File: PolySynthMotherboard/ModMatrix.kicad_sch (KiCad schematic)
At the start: 160 parts, among them SW501 MM, SW502 MM, SW503 MM, SW504 MM, SW505 MM, SW506 MM, SW507 MM, SW508 MM, SW509 MM, SW510 MM, SW511 MM, SW512 MM, SW513 MM, SW514 MM, SW515 MM, SW516 MM, SW517 MM, SW518 MM, SW519 MM, SW520 MM, SW521 MM, SW522 MM, SW523 MM, SW524 MM, SW525 MM, SW526 MM, SW527 MM, SW528 MM, SW529 MM, SW530 MM, SW531 MM, SW532 MM, SW533 MM, SW534 MM, SW535 MM, SW536 MM, SW537 MM, SW538 MM, SW539 MM, SW540 MM, SW541 MM, SW542 MM, SW543 MM, SW544 MM, SW545 MM, SW546 MM, SW547 MM, SW548 MM, U501 MCP23S17_SS

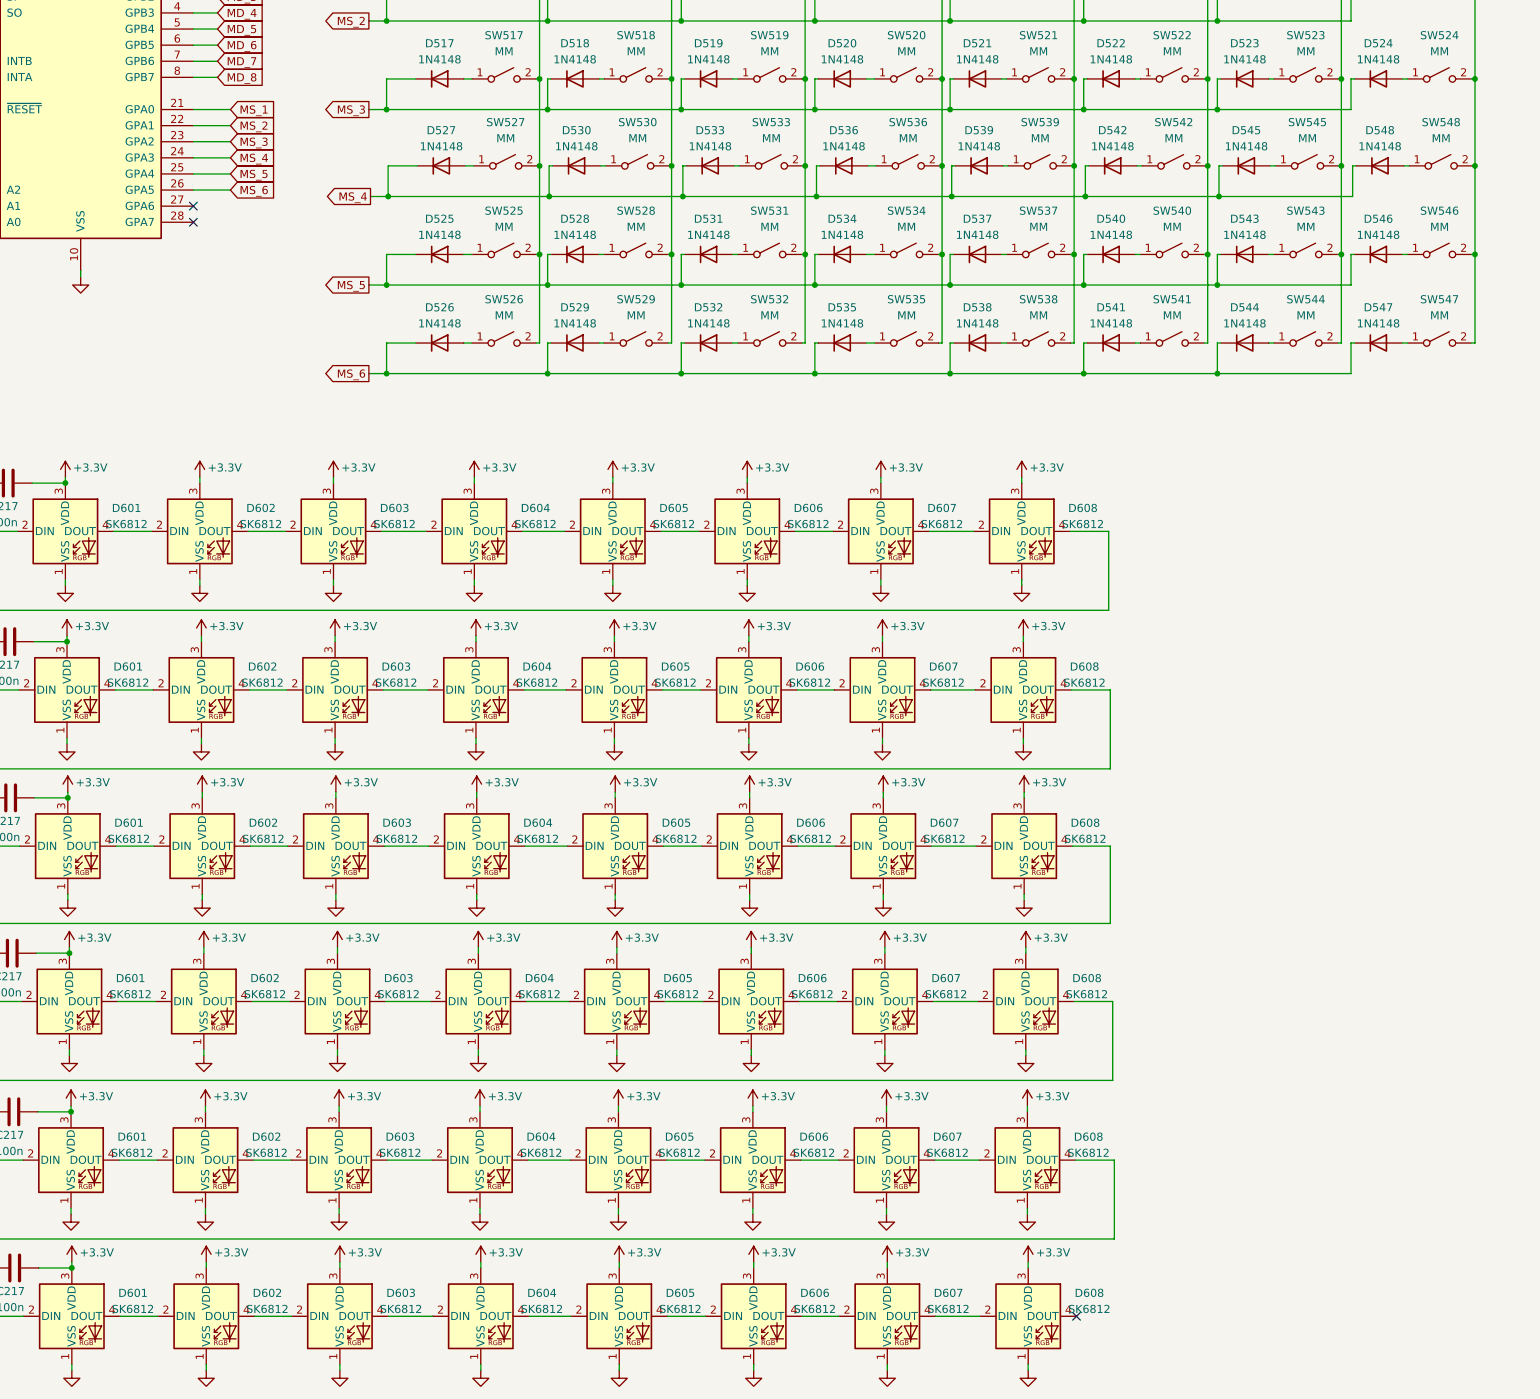
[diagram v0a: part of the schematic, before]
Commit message: net class assignment
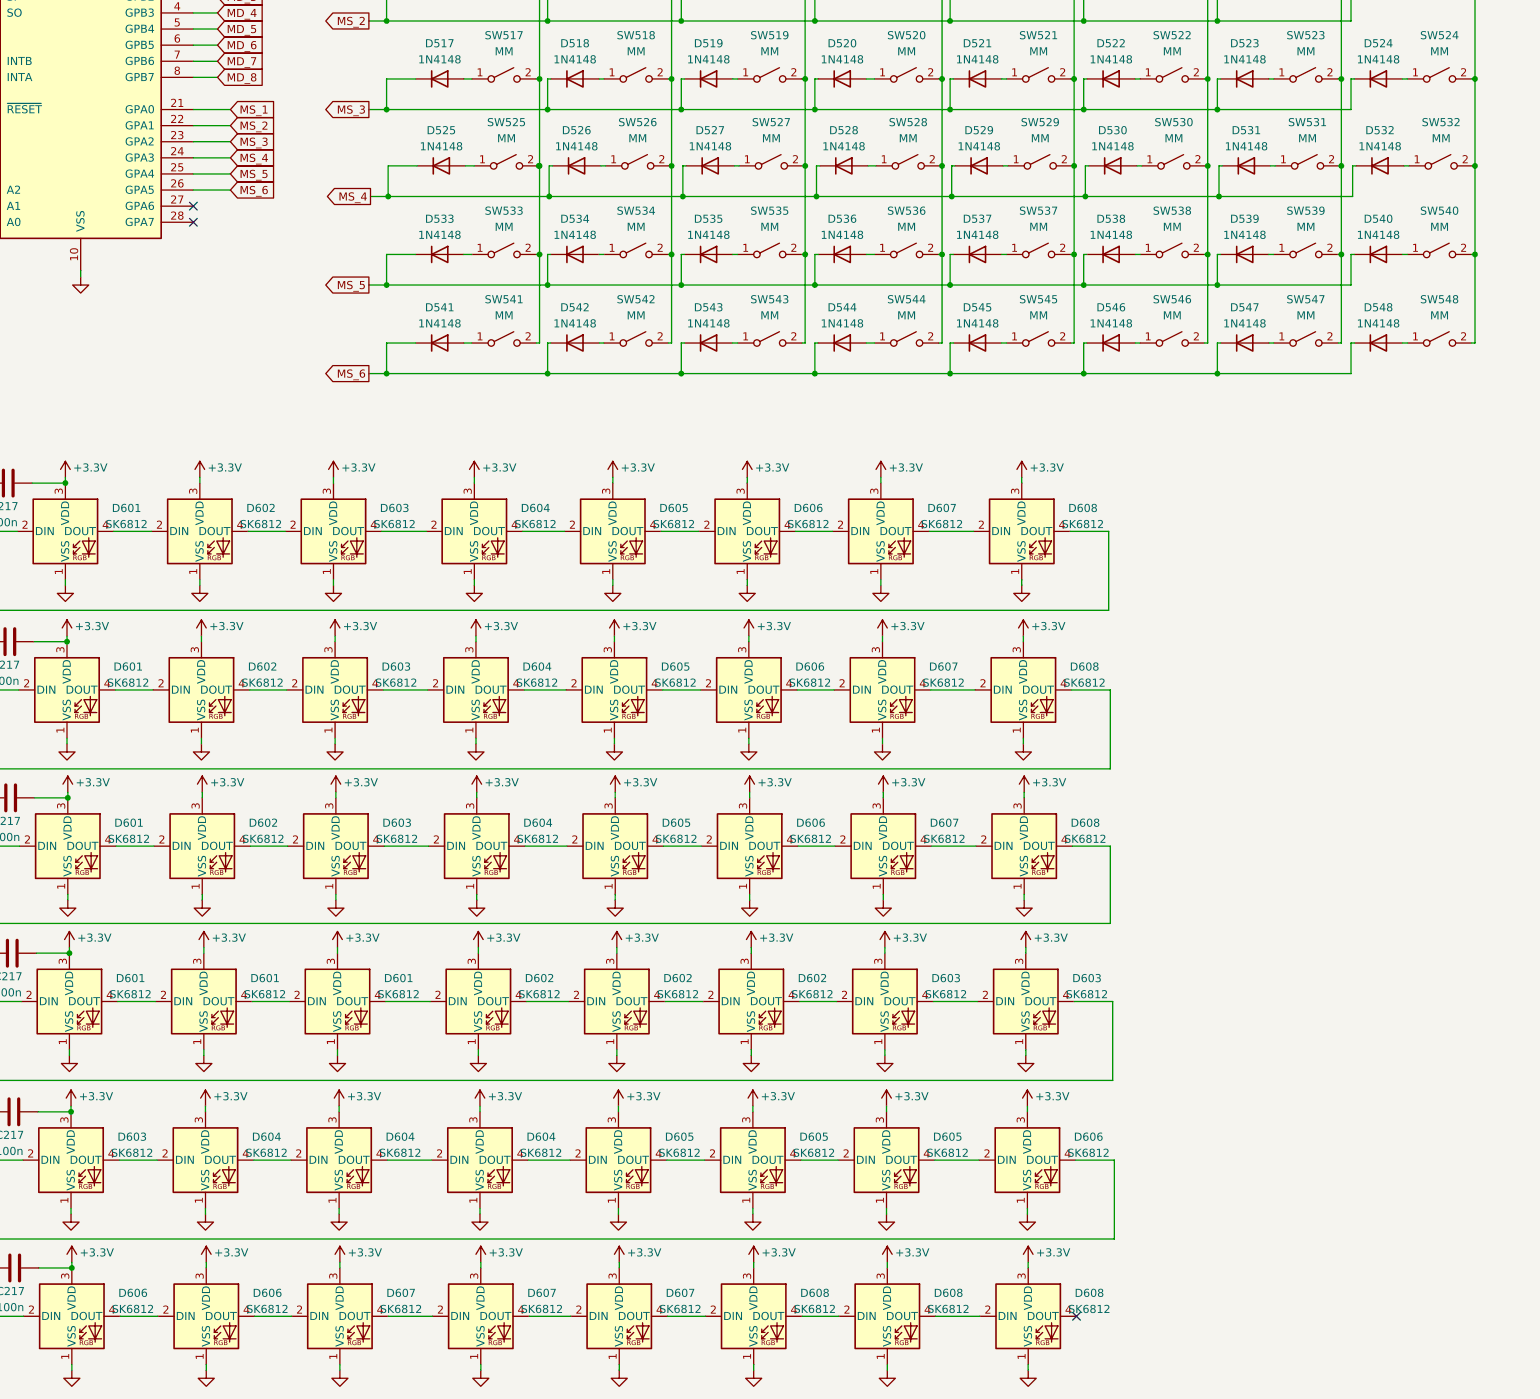
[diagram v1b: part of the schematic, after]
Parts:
- renumbered D527 to D525, D530 to D526, D533 to D527, D536 to D528, D539 to D529, D542 to D530, D545 to D531, D548 to D532, D525 to D533, D528 to D534, D531 to D535, D534 to D536, D540 to D538, D543 to D539, D546 to D540, D526 to D541, D529 to D542, D532 to D543, D535 to D544, D538 to D545, D541 to D546, D544 to D547, D547 to D548
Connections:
- net MD_1: now also SW533.2 (B), SW541.2 (B); no longer SW526.2 (B), SW527.2 (B)
- net MD_2: now also SW526.2 (B), SW534.2 (B), SW542.2 (B); no longer SW528.2 (B), SW529.2 (B), SW530.2 (B)
- net MD_3: now also SW527.2 (B), SW535.2 (B), SW543.2 (B); no longer SW531.2 (B), SW532.2 (B), SW533.2 (B)
- net MD_4: now also SW528.2 (B), SW544.2 (B); no longer SW534.2 (B), SW535.2 (B)
- net MD_5: now also SW529.2 (B), SW545.2 (B); no longer SW538.2 (B), SW539.2 (B)
- net MD_6: now also SW530.2 (B), SW538.2 (B), SW546.2 (B); no longer SW540.2 (B), SW541.2 (B), SW542.2 (B)
- net MD_7: now also SW531.2 (B), SW539.2 (B), SW547.2 (B); no longer SW543.2 (B), SW544.2 (B), SW545.2 (B)
- net MD_8: now also SW532.2 (B), SW540.2 (B); no longer SW546.2 (B), SW547.2 (B)
- net PIXELS_MATRIX: now also D601.2 (DIN); no longer D601.2 (DIN)
- net at D601.2 (DIN): now also D601.4 (DOUT); no longer D608.4 (DOUT)
- net at D601.4 (DOUT): now also D601.2 (DIN); no longer D602.2 (DIN)
- net at D604.2 (DIN): now also D604.4 (DOUT); no longer D603.4 (DOUT)
- net at D604.4 (DOUT): now also D605.2 (DIN); no longer D605.2 (DIN)
- net at SW530.1 (A): now also D530.2 (A); no longer D526.2 (A)
- net at SW545.1 (A): now also D545.2 (A); no longer D531.2 (A)
- net at D529.2 (A): now also SW529.1 (A); no longer SW539.1 (A)
- net at SW541.1 (A): now also D541.2 (A); no longer D546.2 (A)
- net at D605.4 (DOUT): now also D606.2 (DIN); no longer D606.2 (DIN)
- net at D608.4 (DOUT): now also D601.2 (DIN); no longer D601.2 (DIN) (x2)
- net at SW548.1 (A): now also D548.2 (A); no longer D532.2 (A)
- net at SW538.1 (A): now also D538.2 (A); no longer D545.2 (A)
- net at D535.2 (A): now also SW535.1 (A); no longer SW531.1 (A)
- net at SW540.1 (A): now also D540.2 (A); no longer D538.2 (A)
- net at SW527.1 (A): now also D527.2 (A); no longer D525.2 (A)
- net at D539.2 (A): now also SW539.1 (A); no longer SW543.1 (A)
- net at SW546.1 (A): now also D546.2 (A); no longer D540.2 (A)
- net at SW532.1 (A): now also D532.2 (A); no longer D543.2 (A)
- net at D603.2 (DIN): now also D602.4 (DOUT); no longer D602.4 (DOUT)
- net at D603.4 (DOUT): now also D603.2 (DIN); no longer D604.2 (DIN) (x2)
- net at D608.4 (DOUT): now also D608.2 (DIN); no longer D601.2 (DIN)
- net at D601.4 (DOUT): now also D602.2 (DIN); no longer D602.2 (DIN)
- net at SW547.1 (A): now also D547.2 (A); no longer D548.2 (A)
- net at D602.4 (DOUT): now also D602.2 (DIN); no longer D603.2 (DIN)
- net at D536.2 (A): now also SW536.1 (A); no longer SW534.1 (A)
- net at D528.2 (A): now also SW528.1 (A); no longer SW536.1 (A)
- net at SW542.1 (A): now also D542.2 (A); no longer D530.2 (A)
- net at D605.4 (DOUT): now also D605.2 (DIN); no longer D606.2 (DIN) (x2)
- net at D606.4 (DOUT): now also D606.2 (DIN); no longer D607.2 (DIN) (x2)
- net at SW544.1 (A): now also D544.2 (A); no longer D547.2 (A)
- net at SW533.1 (A): now also D533.2 (A); no longer D527.2 (A)
- net at D534.2 (A): now also SW534.1 (A); no longer SW528.1 (A)
- net at SW525.1 (A): now also D525.2 (A); no longer D533.2 (A)
- net at SW526.1 (A): now also D526.2 (A); no longer D541.2 (A)
- net at D607.4 (DOUT): now also D607.2 (DIN); no longer D608.2 (DIN) (x2)
- net at D606.4 (DOUT): now also D607.2 (DIN); no longer D607.2 (DIN)
- net at D604.4 (DOUT): now also D604.2 (DIN); no longer D605.2 (DIN)
- net at D607.4 (DOUT): now also D608.2 (DIN); no longer D608.2 (DIN)
- new net: D602.2 (DIN), D602.4 (DOUT)
- new net: D531.2 (A), SW531.1 (A)
- new net: D543.2 (A), SW543.1 (A)
- new net: D608.2 (DIN), D608.4 (DOUT)
- new net: D603.4 (DOUT), D604.2 (DIN)
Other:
- moved on the sheet: D601, D602, D603, D604, D605, D606, D607, D608, SW525, SW526, SW527, SW528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

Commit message: board layout
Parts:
- D501, D502, D503, D504, D505, D506, D507, D508, D509, D510, D511, D512, D513, D514, D515, D516, D517, D518, D519, D520, D521, D522, D523, D524, D525, D526, D527, D528, D529, D530, D531, D532, D533, D534, D535, D536, D537, D538, D539, D540, D541, D542, D543, D544, D545, D546, D547, D548: footprint Diode_SMD:D_0805_2012Metric -> Diode_SMD:D_SOD-123
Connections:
- net MD_1: now also U501.8 (GPB7); no longer U501.1 (GPB0)
- net MD_2: now also U501.7 (GPB6); no longer U501.2 (GPB1)
- net MD_3: now also U501.6 (GPB5); no longer U501.3 (GPB2)
- net MD_4: now also U501.5 (GPB4); no longer U501.4 (GPB3)
- net MD_5: now also U501.4 (GPB3); no longer U501.5 (GPB4)
- net MD_6: now also U501.3 (GPB2); no longer U501.6 (GPB5)
- net MD_7: now also U501.2 (GPB1); no longer U501.7 (GPB6)
- net MD_8: now also U501.1 (GPB0); no longer U501.8 (GPB7)

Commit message: power supply tweaks
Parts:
- removed D501, D502, D503, D504, D505, D506, D507, D508, D509, D510, D511, D512, D513, D514, D515, D516, D517, D518, D519, D520, D521, D522, D523, D524, D525, D526, D527, D528, D529, D530, D531, D532, D533, D534, D535, D536, D537, D538, D539, D540, D541, D542, D543, D544, D545, D546, D547, D548: 1N4148, Diode_SMD:D_SOD-123, symbol Diode:1N4148
- removed SW515, SW516, SW517, SW518, SW519, SW520, SW521, SW522, SW523, SW524, SW525, SW526, SW527, SW528, SW529, SW530, SW531, SW532, SW533, SW534, SW535, SW536, SW537, SW538, SW539, SW540, SW541, SW542, SW543, SW544, SW545, SW546, SW547, SW548: MM, Button_Switch_THT:SW_PUSH_6mm, symbol Switch:SW_SPST
- added R509, R510, R511, R512, R513, R514: 47k, PCM_Resistor_SMD_AKL:R_0805_2012Metric, symbol Device:R_US
- SW501: value MM -> MD1
- SW502: value MM -> MD2
- SW503: value MM -> MD3
- SW504: value MM -> MD4
- SW505: value MM -> MD5
- SW506: value MM -> MD6
- SW507: value MM -> MD7
- SW508: value MM -> MD8
- SW509: value MM -> MS1
- SW510: value MM -> MS2
- SW511: value MM -> MS3
- SW512: value MM -> MS4
- SW513: value MM -> MS5
- SW514: value MM -> MS6
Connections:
- net +3.3V: now also R509.1, R510.1, R511.1, R512.1, R513.1, R514.1
- net GND: now also SW501.1 (A), SW502.1 (A), SW503.1 (A), SW504.1 (A), SW505.1 (A), SW506.1 (A), SW507.1 (A), SW508.1 (A), SW509.1 (A), SW510.1 (A), SW511.1 (A), SW512.1 (A), SW513.1 (A), SW514.1 (A)
- net MD_1: no longer SW509.2 (B)
- net MD_2: no longer SW510.2 (B)
- net MD_3: no longer SW511.2 (B)
- net MD_4: no longer SW512.2 (B)
- net MD_5: no longer SW513.2 (B)
- net MD_6: no longer SW514.2 (B)
- net MS_1: now also SW509.2 (B), R509.2
- net MS_2: now also SW510.2 (B), R510.2
- net MS_3: now also SW511.2 (B), R511.2
- net MS_4: now also SW512.2 (B), R512.2
- net MS_5: now also SW513.2 (B), R513.2
- net MS_6: now also SW514.2 (B), R514.2

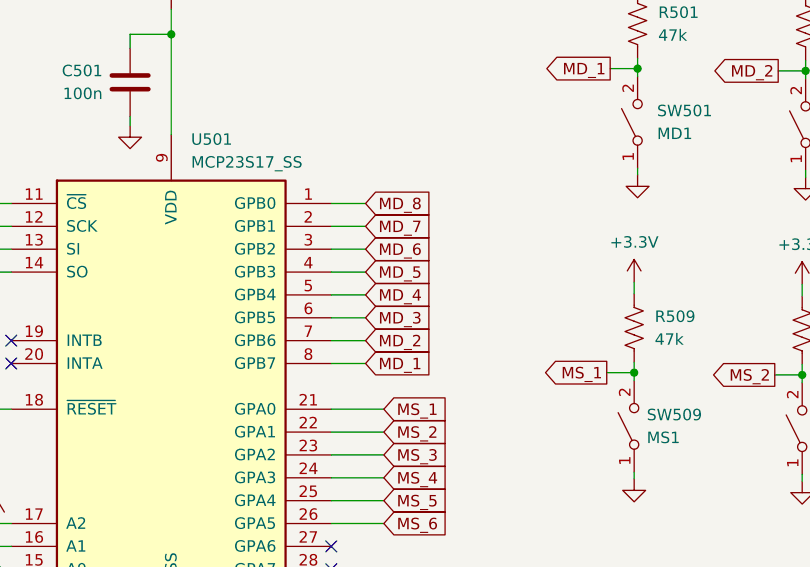
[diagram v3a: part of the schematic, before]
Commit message: footprints placed
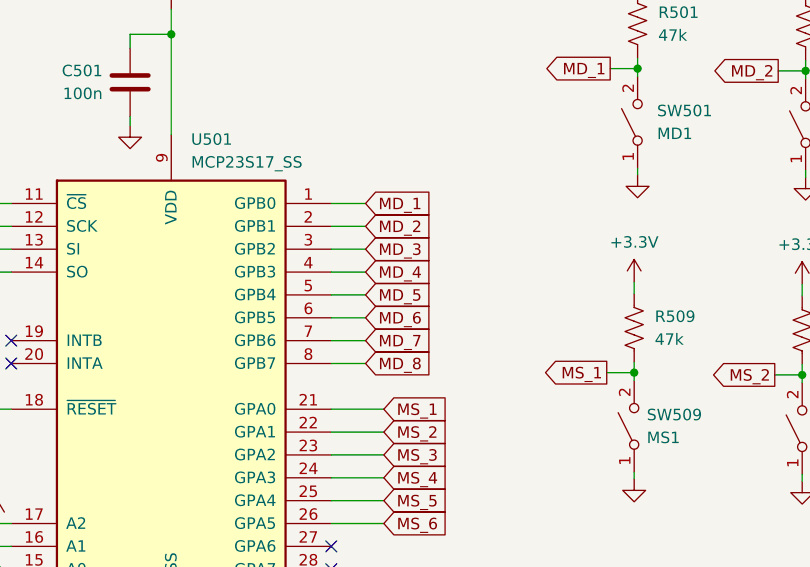
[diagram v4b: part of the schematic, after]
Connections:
- net MD_1: now also U501.1 (GPB0); no longer U501.8 (GPB7)
- net MD_2: now also U501.2 (GPB1); no longer U501.7 (GPB6)
- net MD_3: now also U501.3 (GPB2); no longer U501.6 (GPB5)
- net MD_4: now also U501.4 (GPB3); no longer U501.5 (GPB4)
- net MD_5: now also U501.5 (GPB4); no longer U501.4 (GPB3)
- net MD_6: now also U501.6 (GPB5); no longer U501.3 (GPB2)
- net MD_7: now also U501.7 (GPB6); no longer U501.2 (GPB1)
- net MD_8: now also U501.8 (GPB7); no longer U501.1 (GPB0)
